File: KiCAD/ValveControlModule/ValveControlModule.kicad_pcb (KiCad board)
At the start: 2 copper layers, 90 x 70 mm, 21 parts, among them J1 DF51A-4P-2DS, J2 DF11-8DP-2DS, U1 XIAO-RP2040-DIP, U2 LT1785xS8, U3 MCP2515-xSO, U4 MCP2562-E-SN, Y1 8MHz

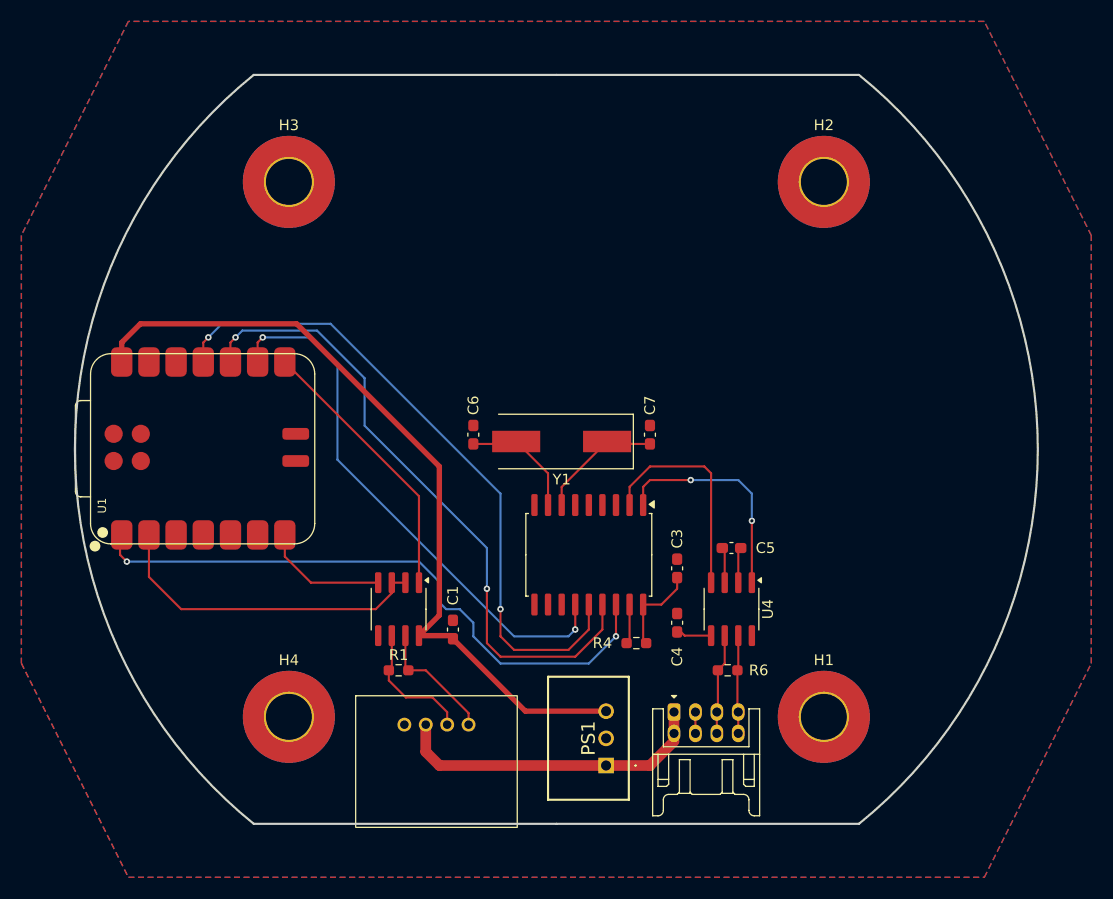
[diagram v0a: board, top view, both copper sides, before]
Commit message: 電源，RS485の仕様を確定
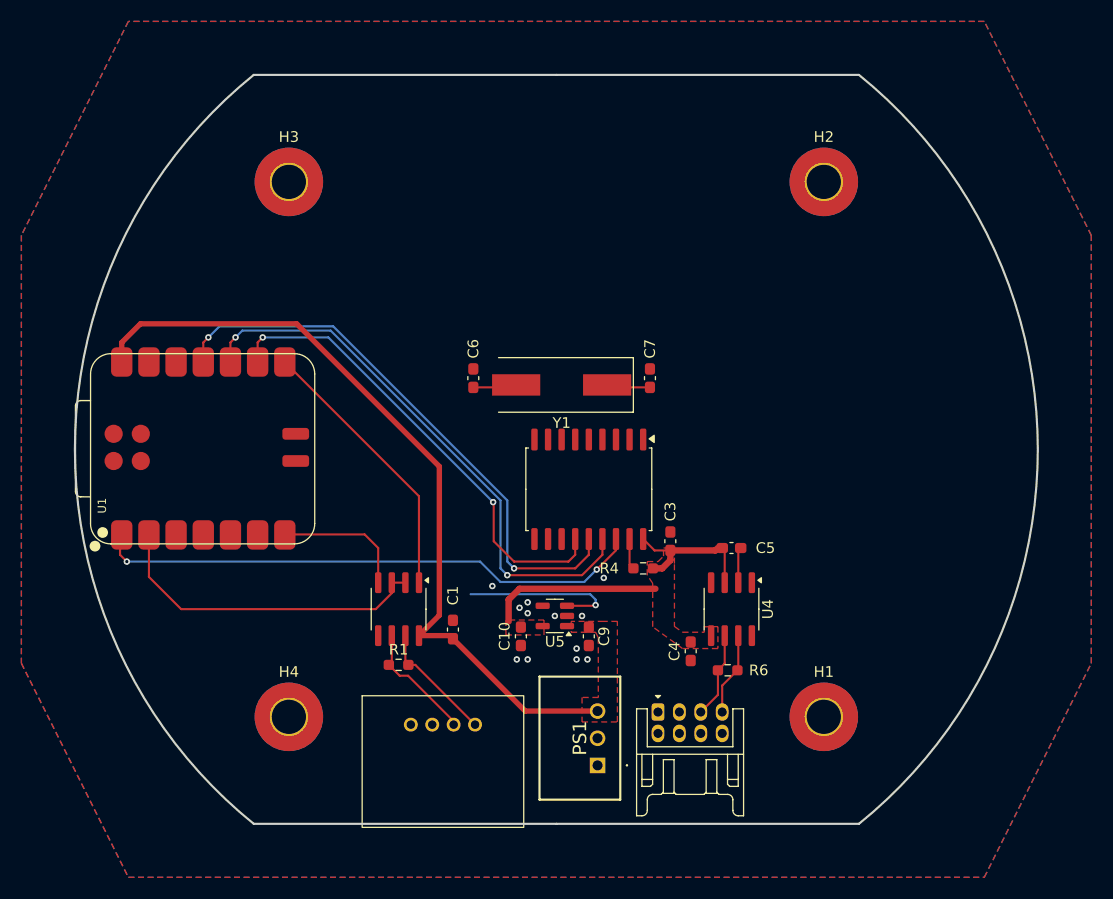
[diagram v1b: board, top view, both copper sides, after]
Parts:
- added C10: 1u, Capacitor_SMD:C_0603_1608Metric_Pad1.08x0.95mm_HandSolder, F.Cu at (146.7, 117.5)
- added C9: 1u, Capacitor_SMD:C_0603_1608Metric_Pad1.08x0.95mm_HandSolder, F.Cu at (153.0, 117.5)
- added U5: NCV8114BSN330T1G, Package_TO_SOT_SMD:TSOT-23-5, F.Cu at (149.9, 115.6)
- H1, H2, H3, H4: footprint MountingHole:MountingHole_4.3mm_M4_Pad_TopBottom -> MountingHole:MountingHole_3.2mm_M3_Pad_TopBottom
- moved R4 7.01 mm to (158.1, 111.1)
- moved U3 6.12 mm to (153.0, 103.7)
- moved C6 5.28 mm to (142.2, 93.3)
- moved C7 5.28 mm to (158.8, 93.3)
- moved Y1 5.28 mm to (150.5, 94.0)
- moved C4 2.95 mm to (162.6, 118.9), turned to 90 degrees
- moved C3 2.62 mm to (160.7, 108.6)
- moved J2 1.50 mm to (162.5, 128.0)
- moved PS1 0.80 mm to (153.8, 129.5)
- moved J1 0.61 mm to (139.4, 135.2)
- moved R1 0.51 mm to (135.3, 120.1)
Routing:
- net +12V: track 30.0 -> 0.00 mm
- net CAN_TX: track 21.0 -> 0.00 mm, vias 2 -> 0
- net CAN_RX: track 20.6 -> 0.00 mm
- net RT9080_EN: track 0.00 -> 15.1 mm, vias 0 -> 1
- net +3.3V: track 15.2 -> 30.3 mm
- net SPI_MOSI: track 62.1 -> 53.2 mm
- net SPI_MISO: track 60.9 -> 52.5 mm
- net OSC2: track 11.8 -> 4.10 mm
- net OSC1: track 11.3 -> 4.10 mm
- net SPI_SCK: track 51.1 -> 44.2 mm
- net SPI_CS_MCP2515: track 58.4 -> 51.6 mm
- net GND: track 5.33 -> 3.33 mm, vias 0 -> 12
- net CAN_H: track 9.20 -> 7.76 mm
- net CAN_L: track 9.44 -> 8.07 mm
- net Net-(U3-~{RESET}): track 3.72 -> 2.89 mm
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- added copper zone on F.Cu, net +3.3V
- added copper zone on F.Cu, net +5V

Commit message: 基本的な機能が完成
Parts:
- moved C1 1.91 mm to (139.2, 118.4), turned to 90 degrees
- moved C6 0.64 mm to (141.6, 93.3)
- moved C7 0.63 mm to (158.1, 93.3)
- moved Y1 0.63 mm to (149.9, 94.0)
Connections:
- U5 pad 3: RT9080_EN -> +5V
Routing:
- net CAN_RX: track 0.00 -> 22.3 mm, vias 0 -> 2
- net CAN_TX: track 0.00 -> 21.8 mm
- net RT9080_EN: track 15.1 -> 0.00 mm, vias 1 -> 0
- net OSC2: track 4.10 -> 10.7 mm
- net OSC1: track 4.10 -> 10.7 mm
- net +5V: track 74.0 -> 78.8 mm, vias 0 -> 2
- net +12V: track 0.00 -> 2.00 mm
- net GND: vias 12 -> 23
- added copper zone on F.Cu, net +12V
